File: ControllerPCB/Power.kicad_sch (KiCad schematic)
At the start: 0 parts

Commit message: Power_Connector
Power portion added
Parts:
- added C23: 10u, symbol Device:C
- added C24: 1u, symbol Device:C
- added D1: RED, symbol Device:LED
- added J2: ASMPR45-1X2-RK, ASMPR45-1X2-RK:APP_ASMPR45-1X2-RK, symbol Power_Connector:ASMPR45-1X2-RK
- added R83: 1k, Resistor_SMD:R_1206_3216Metric, symbol Device:R
- added U1: LT1763CS8-3.3PBF, LT1763CS8-3.3PBF:SOIC127P600X175-8N, symbol 3.3_LDO:LT1763CS8-3.3PBF
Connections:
- new net: D1.1 (K), R83.2
- new net +3.3V: C23.1, D1.2 (A), U1.1 (OUT), U1.2 (SENSE), U1.5 (~SHDN)
- new net GND: C23.2, C24.2, J2.2, R83.1, U1.3 (GND_2), U1.6 (GND), U1.7 (GND_3)
- new net V_IN: C24.1, J2.1, U1.8 (IN)
- no-connect marks 0 -> 1

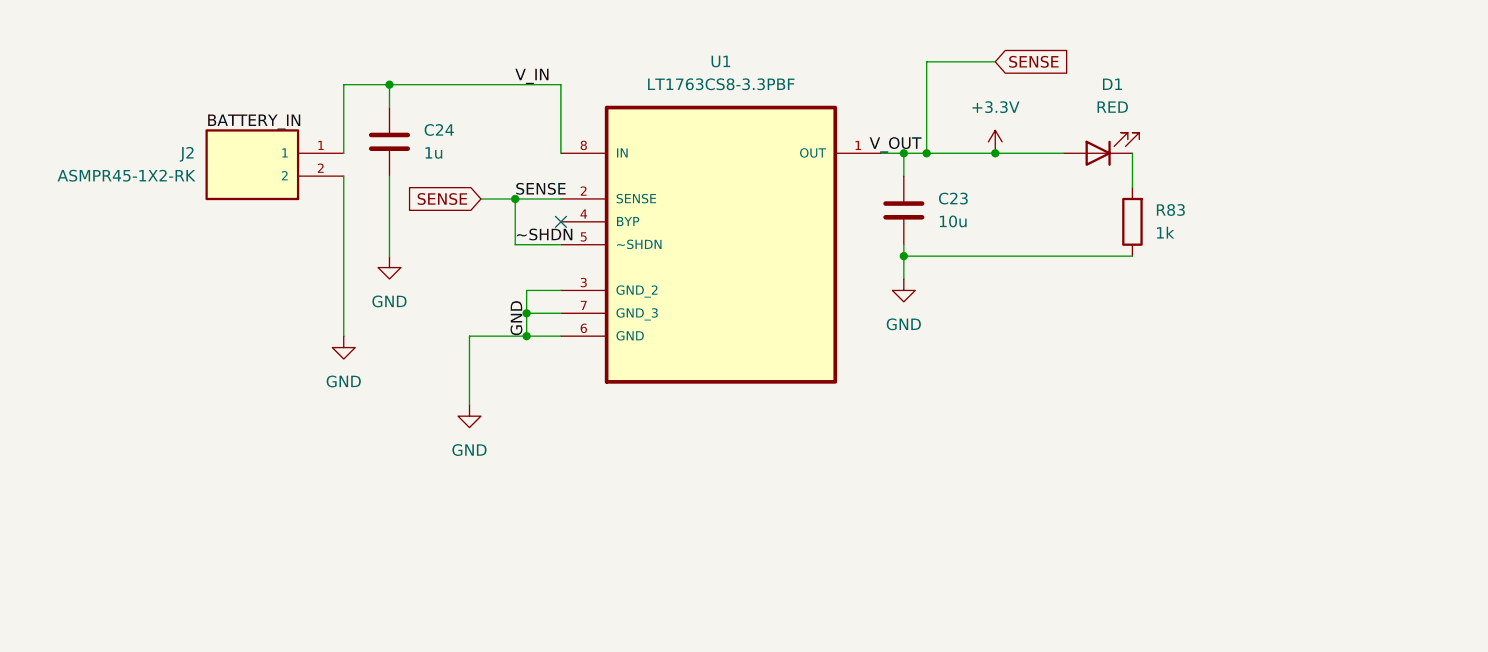
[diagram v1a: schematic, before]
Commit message: rev 0.1
- power and amplitude sheets added
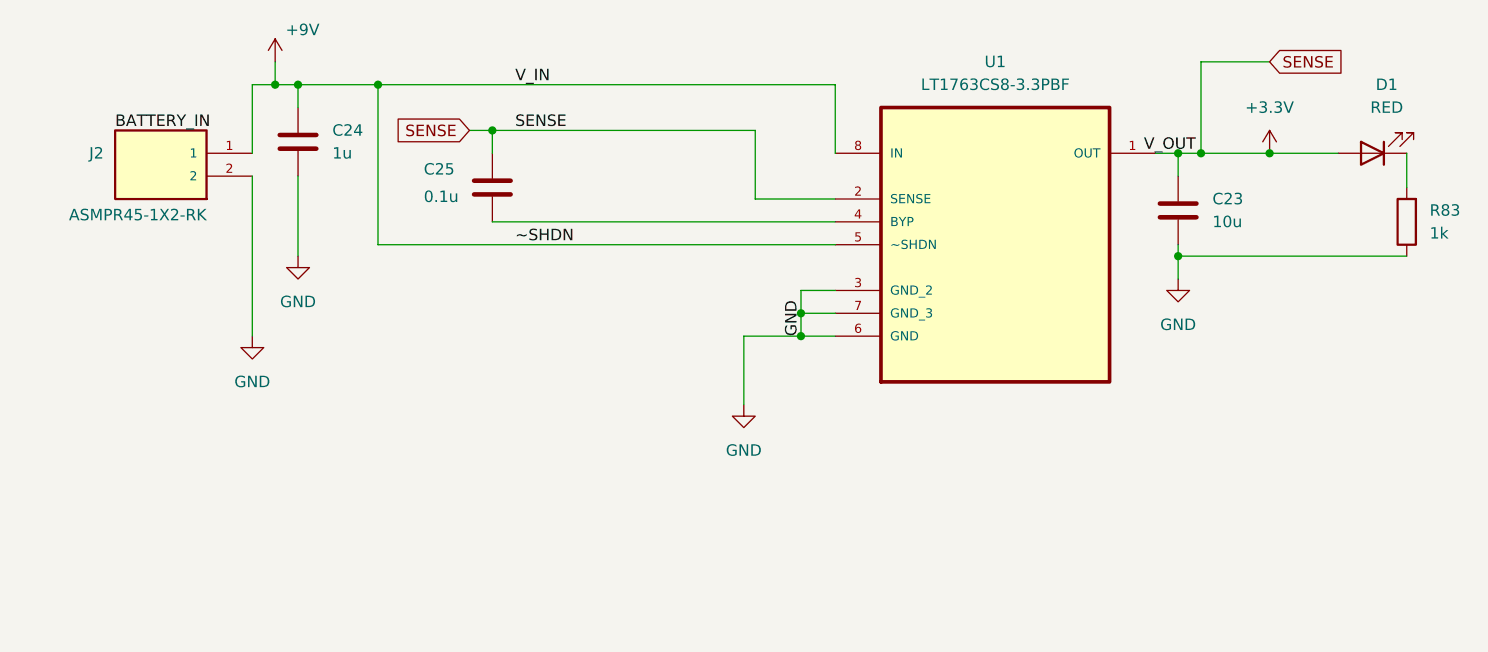
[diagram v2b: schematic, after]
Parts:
- added C25: 0.1u, symbol Device:C
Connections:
- net +3.3V: now also C25.1; no longer U1.5 (~SHDN)
- net at U1.4 (BYP): now also C25.2
- net V_IN renamed +9V
- net +9V: now also U1.5 (~SHDN)
- no-connect marks 1 -> 0
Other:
- moved on the sheet: C23, C24, D1, J2, R83, U1

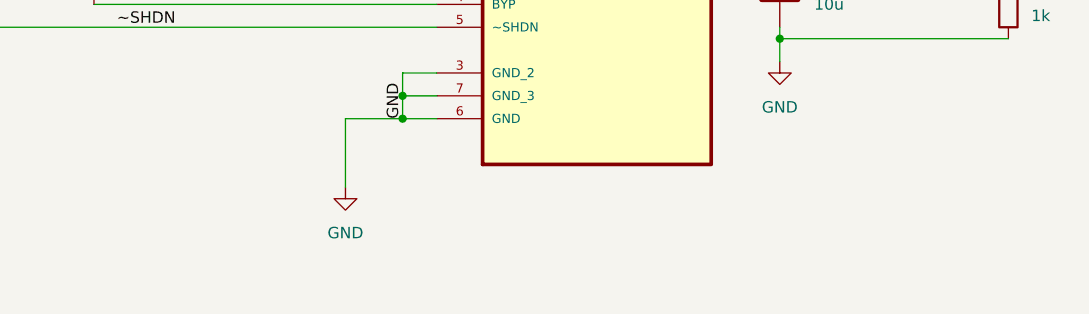
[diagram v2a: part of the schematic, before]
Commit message: rev 0.1 - Redid the GPIO pinouts and removed the CLRs. - Split the 80 pin conn into two 40 pin conns - Added conn and pinouts for SWD - Added conn and pinouts for USB_FS over USB Micro B - Added conn for the MIDI Controls and Piezo pickup
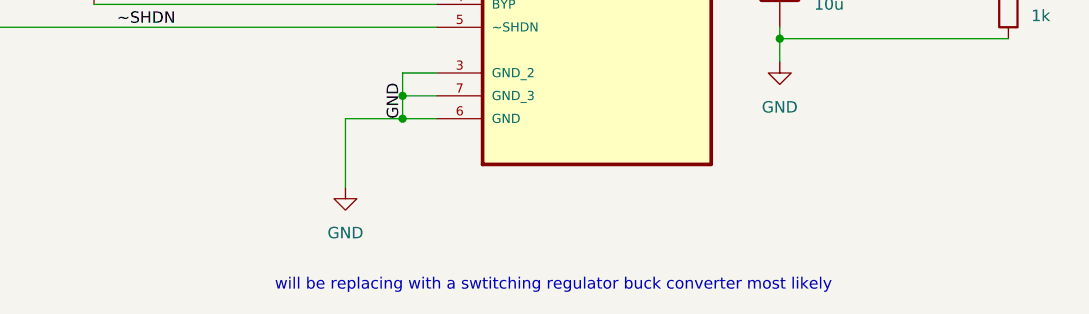
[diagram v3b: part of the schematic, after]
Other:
- note added: "will be replacing with a swtitching regulator buck converter most likely"
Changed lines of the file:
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@@
+		)
+	)
+	(text "will be replacing with a swtitching regulator buck converter most likely"
+		(exclude_from_sim no)
+		(at 115.824 66.802 0)
+		(effects
+			(font
+				(size 1.27 1.27)
+			)
 		)
 	)

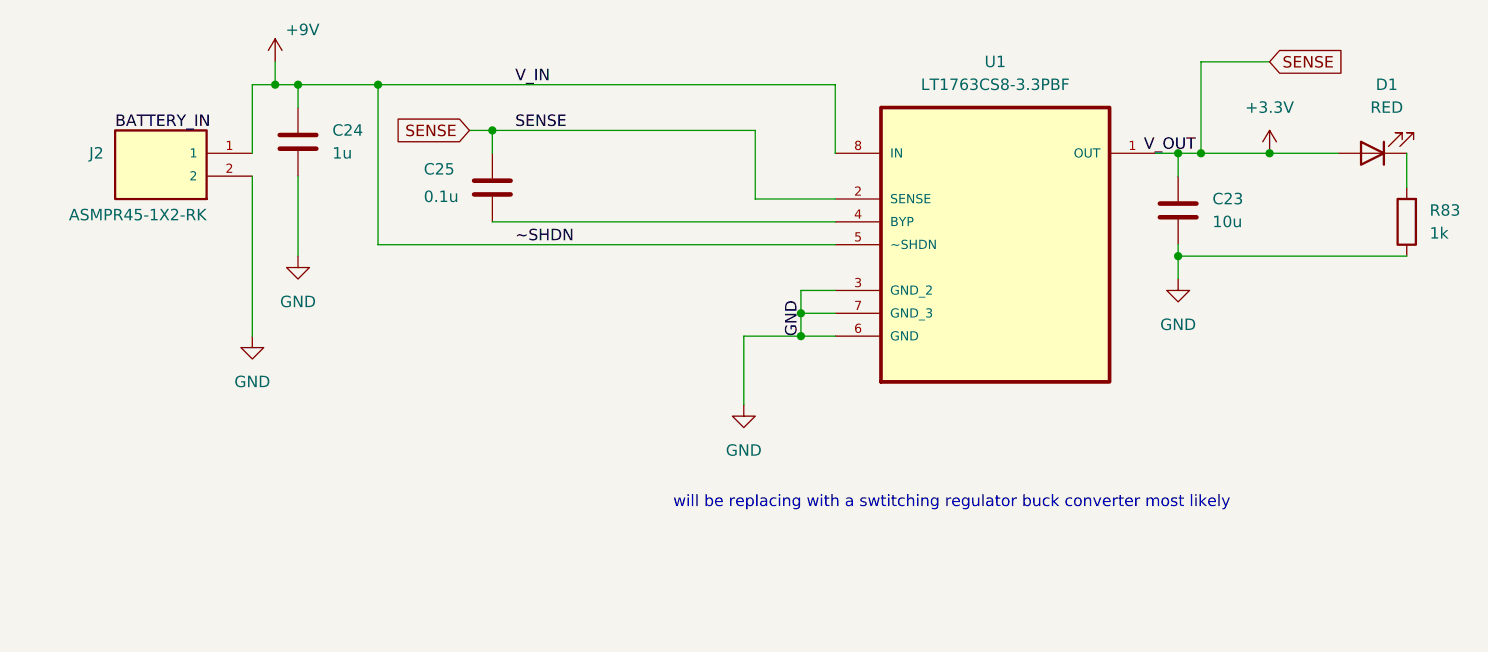
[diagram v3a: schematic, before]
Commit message: Redid the power supply schematic. Controller now powered from the 5V supply from the usb VBUS. Also added EMD suppression TVS diode to the VBUS line to avoid any possible voltage surge.
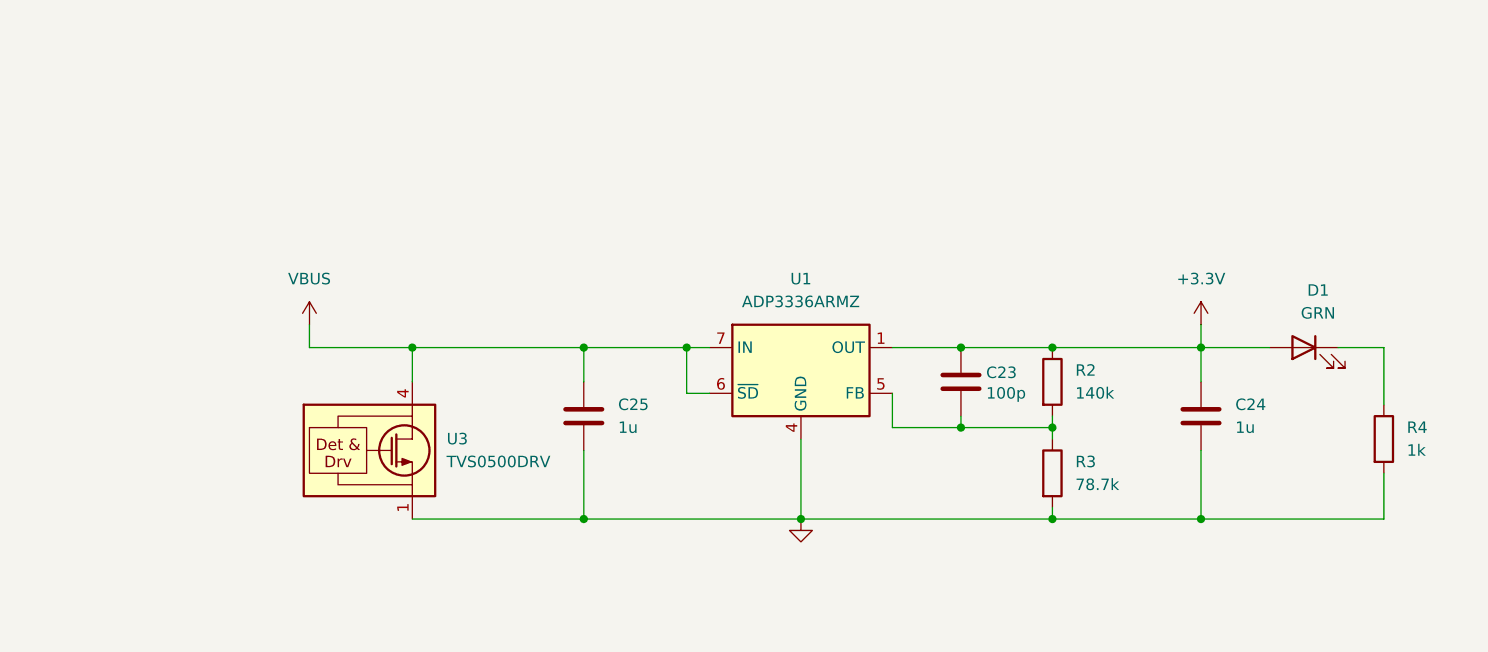
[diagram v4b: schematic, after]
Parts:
- removed J2: ASMPR45-1X2-RK, ASMPR45-1X2-RK:APP_ASMPR45-1X2-RK, symbol Power_Connector:ASMPR45-1X2-RK
- removed R83: 1k, Resistor_SMD:R_1206_3216Metric, symbol Device:R
- removed U1: LT1763CS8-3.3PBF, LT1763CS8-3.3PBF:SOIC127P600X175-8N, symbol 3.3_LDO:LT1763CS8-3.3PBF
- added R2: 140k, symbol Device:R
- added R3: 78.7k, symbol Device:R
- added R4: 1k, symbol Device:R
- added U1: ADP3336ARMZ, Package_SO:MSOP-8_3x3mm_P0.65mm, symbol Regulator_Linear:ADP3336ARMZ
- added U3: TVS0500DRV, Package_SON:WSON-6-1EP_2x2mm_P0.65mm_EP1x1.6mm, symbol Power_Protection:TVS0500DRV
- C23: value 10u -> 100p
- C25: value 0.1u -> 1u
- D1: value RED -> GRN
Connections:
- net +9V is gone; now on net +3.3V: C24.1
- net +3.3V: now also R2.1, U1.1 (OUT), U1.2 (OUT), U1.3 (OUT); no longer C25.1
- net GND: now also C25.2, R3.2, R4.2, U1.4 (GND), U3.1 (GND), U3.2 (GND), U3.3 (GND), U3.7 (GND); no longer C23.2
- net at D1.1 (K): now also R4.1
- new net: C23.2, R2.2, R3.1, U1.5 (FB)
- new net VBUS: C25.1, U1.6 (~{SD}), U1.7 (IN), U1.8 (IN), U3.4 (IN), U3.5 (IN), U3.6 (IN)
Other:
- note removed: "will be replacing with a swtitching regulator buck converter most likely"
- title: (none) -> MCU 3.3V Power Supply

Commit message: Updated many things.
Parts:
- removed U3: TVS0500DRV, Package_SON:WSON-6-1EP_2x2mm_P0.65mm_EP1x1.6mm, symbol Power_Protection:TVS0500DRV
- added D5: BAT_TVS, symbol Device:D_TVS
- added J13: +9V Power Conn, symbol Connector:Conn_01x02_Pin
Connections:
- net GND: now also D5.1 (A1), J13.2 (Pin_2)
- net VBUS: no longer names the net of C25.1, U1.6 (~{SD}), U1.7 (IN), U1.8 (IN)
- net VBUS: now also D5.2 (A2), J13.1 (Pin_1)
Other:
- note added: "3-644343-2"
- note added: "A113510-ND"
- note added: "External Connector For Power"
- note added: "TPSMB10CA"

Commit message: Organized the schematic a bit
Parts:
- C23, C24, C25: footprint (none) -> Capacitor_SMD:C_01005_0402Metric
- D1: footprint (none) -> LED_SMD:LED_0603_1608Metric
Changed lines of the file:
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@@
 			)
 		)
-		(property "Footprint" ""
+		(property "Footprint" "Capacitor_SMD:C_01005_0402Metric"
 			(at 75.8952 60.96 0)
 			(effects
@@
 			)
 		)
-		(property "Footprint" ""
+		(property "Footprint" "Capacitor_SMD:C_01005_0402Metric"
 			(at 117.8052 57.15 0)
 			(effects
@@
 			)
 		)
-		(property "Footprint" ""
+		(property "Footprint" "Capacitor_SMD:C_01005_0402Metric"
 			(at 144.4752 60.96 0)
 			(effects
@@
 			)
 		)
-		(property "Footprint" ""
+		(property "Footprint" "LED_SMD:LED_0603_1608Metric"
 			(at 154.94 49.53 0)
 			(effects

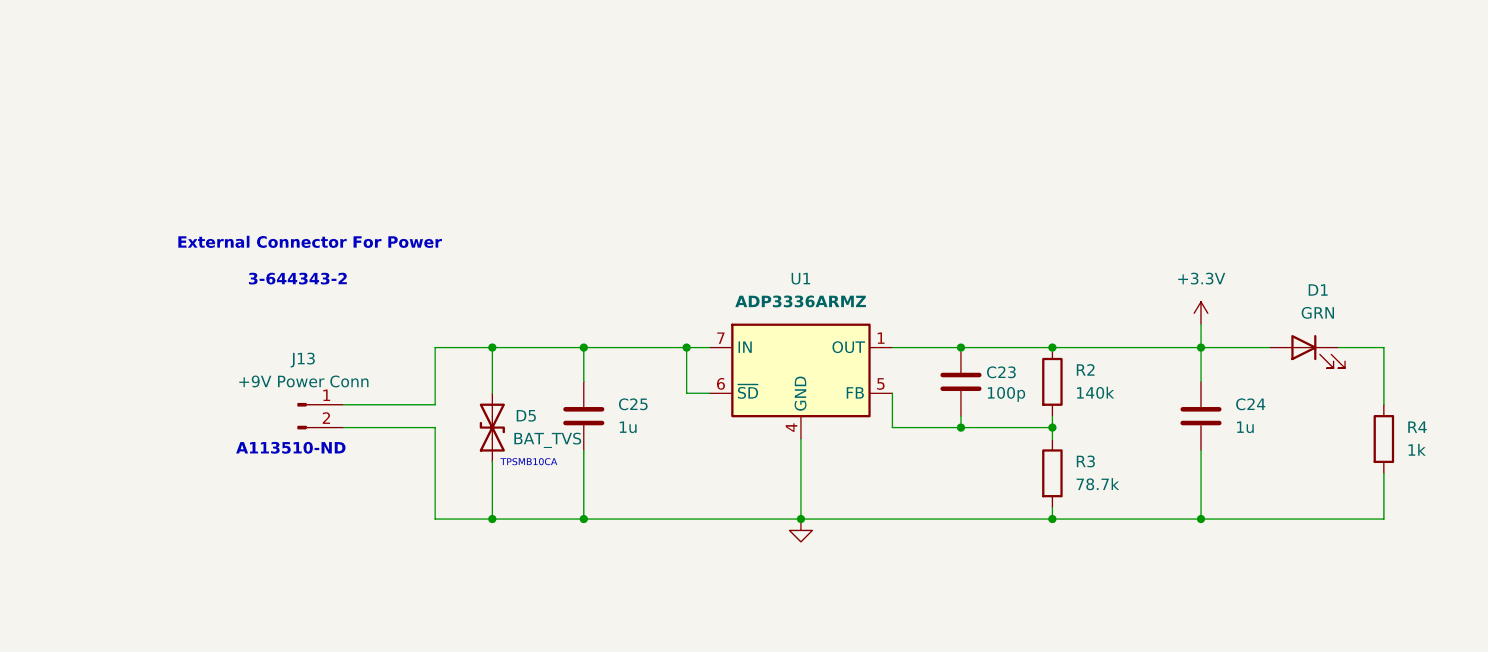
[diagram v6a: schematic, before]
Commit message: Began the PCB. Placed the decoupling caps, usb micro b conn and others. Adding footprints for components as well.
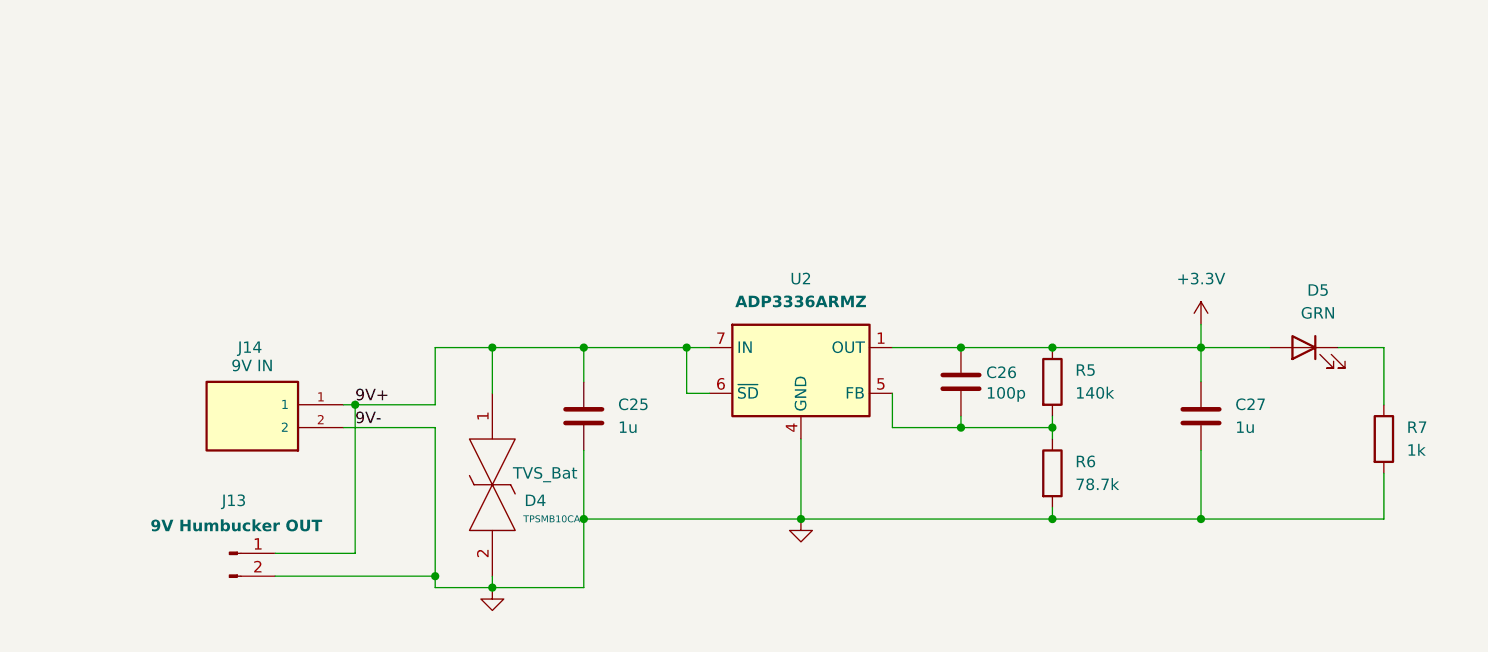
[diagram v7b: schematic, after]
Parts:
- removed D5: BAT_TVS, symbol Device:D_TVS
- added D4: TVS_Bat, TPSMB10CA:DIONM5436X244N, symbol TPSMB10CA:TPSMB10CA
- added J14: 9V IN, PowerConnector:APP_ASMPR45-1X2-RK, symbol ASMPR45-1X2-RK:ASMPR45-1X2-RK
- C25: footprint Capacitor_SMD:C_01005_0402Metric -> Capacitor_SMD:C_0402_1005Metric
- C26: renamed from C23; footprint Capacitor_SMD:C_01005_0402Metric -> Capacitor_SMD:C_0402_1005Metric
- C27: renamed from C24; footprint Capacitor_SMD:C_01005_0402Metric -> Capacitor_SMD:C_0402_1005Metric
- J13: value +9V Power Conn -> 9V Humbucker OUT; footprint (none) -> 3_641126_2:TE_3-641126-2
- R5: renamed from R2; footprint (none) -> Resistor_SMD:R_0402_1005Metric
- R6: renamed from R3; footprint (none) -> Resistor_SMD:R_0402_1005Metric
- R7: renamed from R4; footprint (none) -> Resistor_SMD:R_0402_1005Metric
- U2: renamed from U1; footprint Package_SO:MSOP-8_3x3mm_P0.65mm -> ADP3336ARMZ_REEL7:RM_8_ADI
- renumbered D1 to D5
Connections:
- net GND: now also C25.1, J13.1 (Pin_1), U2.6 (~{SD}), U2.7 (IN), U2.8 (IN), D4.1, D4.2, J14.1, J14.2
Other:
- note removed: "3-644343-2"
- note removed: "A113510-ND"
- note removed: "External Connector For Power"

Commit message: Added separate sheet for IO. Added TVS diodes for every external input to the controller except for the ADC and MIDI control inputs. Still need to add decoupling caps for the 9V humbucker source. Parts were chosen with JLPCB library stock in mind. Replaced the 8MHz crystal with a 16MHz crystal.
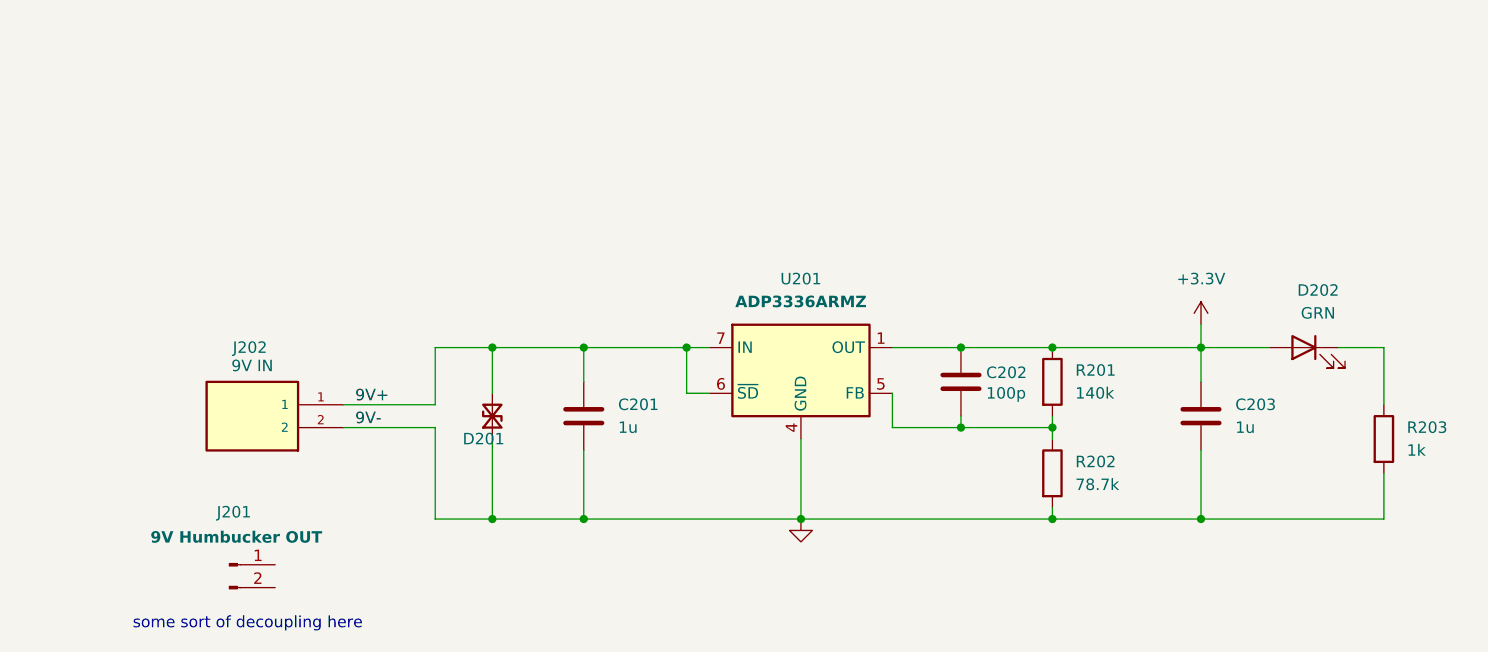
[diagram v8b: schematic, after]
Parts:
- removed D4: TVS_Bat, TPSMB10CA:DIONM5436X244N, symbol TPSMB10CA:TPSMB10CA
- added D201: D_TVS_Small, symbol Device:D_TVS_Small
- renumbered C25 to C201, C26 to C202, C27 to C203, D5 to D202, J13 to J201, J14 to J202, R5 to R201, R6 to R202, R7 to R203, U2 to U201
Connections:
- net GND: now also D201.1 (A1); no longer C201.1, J201.1 (Pin_1), J201.2 (Pin_2), J202.1, U201.6 (~{SD}), U201.7 (IN), U201.8 (IN)
- new net 9V+: C201.1, D201.2 (A2), J202.1, U201.6 (~{SD}), U201.7 (IN), U201.8 (IN)
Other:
- note added: "some sort of decoupling here"
- note removed: "TPSMB10CA"
- moved on the sheet: J201
